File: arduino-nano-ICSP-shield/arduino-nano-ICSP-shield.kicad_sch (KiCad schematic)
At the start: 9 parts, among them J1 Analog, J2 Digital, J3 AVR-ISP-6, J4 Conn_02x04_Counter_Clockwise

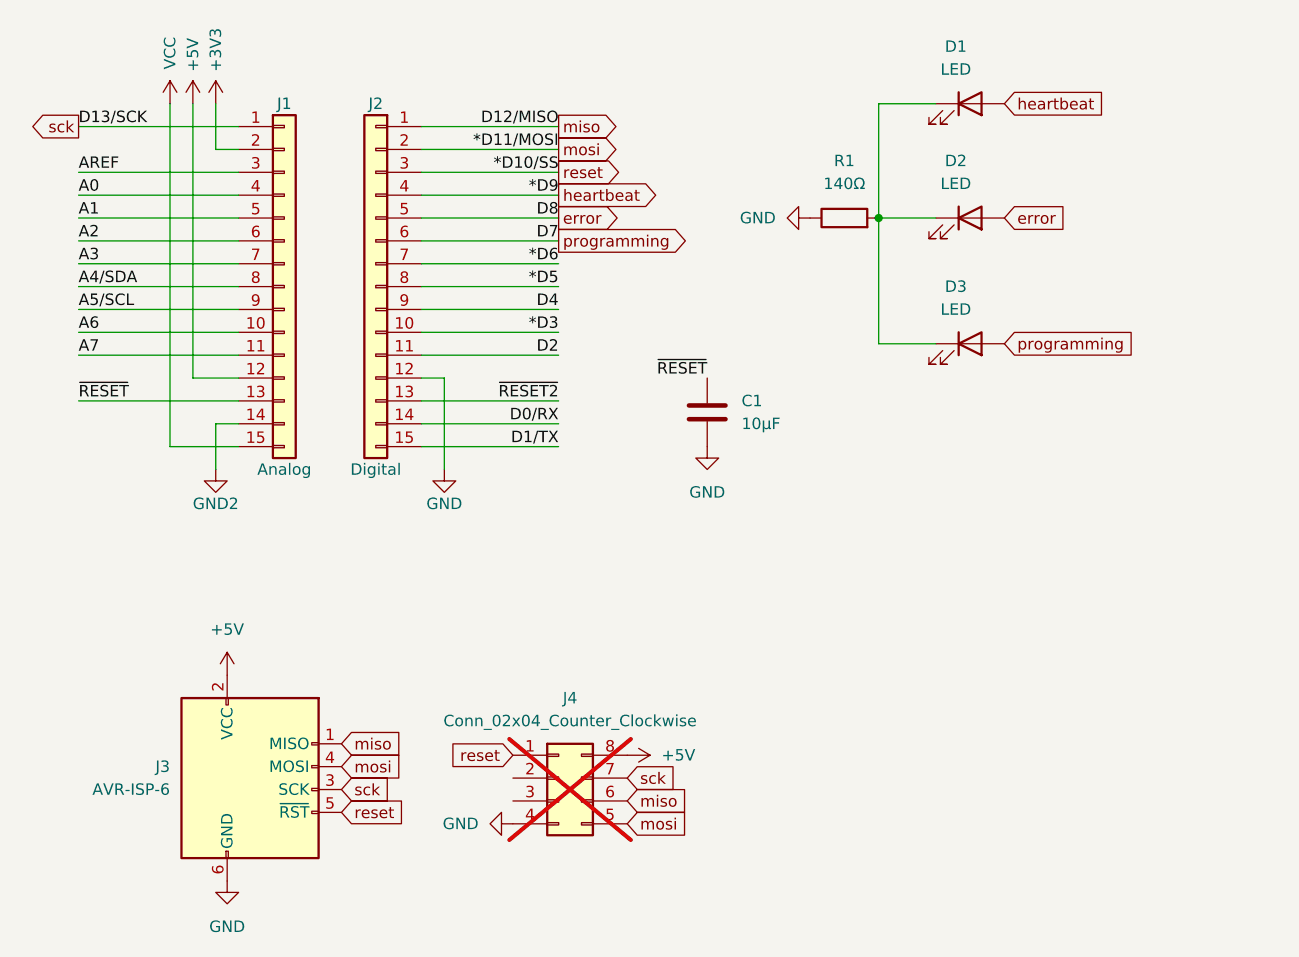
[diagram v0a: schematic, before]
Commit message: add no_connect
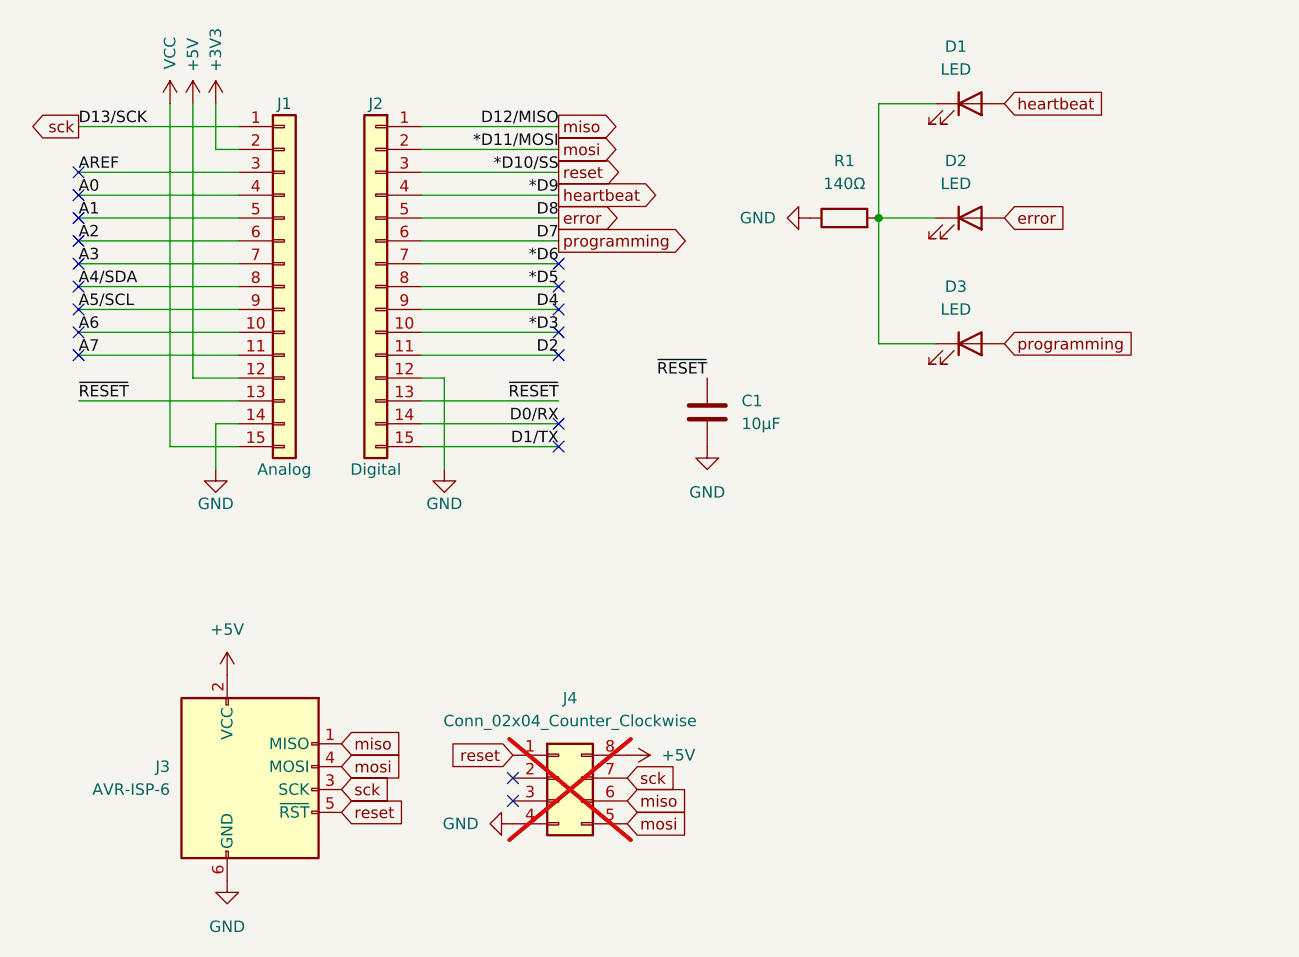
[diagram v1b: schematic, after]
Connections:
- net GND2 is gone; now on net GND: J1.14 (Pin_14)
- net ~{RESET2} is gone; now on net ~{RESET}: J2.13 (Pin_13)
- no-connect marks 0 -> 18
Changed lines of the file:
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@@
 		(color 0 0 0 0)
+	)
+	(no_connect
+		(at 17.78 41.91)
+	)
+	(no_connect
+		(at 71.12 49.53)
+	)
+	(no_connect
+		(at 71.12 41.91)
+	)
+	(no_connect
+		(at 17.78 52.07)
+	)
+	(no_connect
+		(at 71.12 46.99)
+	)
+	(no_connect
+		(at 66.04 99.06)
+	)
+	(no_connect
+		(at 66.04 101.6)
+	)
+	(no_connect
+		(at 71.12 52.07)
+	)
+	(no_connect
+		(at 17.78 49.53)
+	)
+	(no_connect
+		(at 17.78 39.37)
+	)
+	(no_connect
+		(at 17.78 34.29)
+	)
+	(no_connect
+		(at 17.78 46.99)
+	)
+	(no_connect
+		(at 71.12 62.23)
+	)
+	(no_connect
+		(at 71.12 44.45)
+	)
+	(no_connect
+		(at 71.12 59.69)
+	)
+	(no_connect
+		(at 17.78 36.83)
+	)
+	(no_connect
+		(at 17.78 44.45)
+	)
+	(no_connect
+		(at 17.78 31.75)
 	)
 	(wire
@@
 		)
 	)
-	(label "~{RESET2}"
+	(label "~{RESET}"
 		(at 71.12 57.15 180)
 		(effects
@@
 			)
 		)
-		(property "Value" "GND2"
+		(property "Value" "GND"
 			(at 33.02 68.58 0)
 			(effects

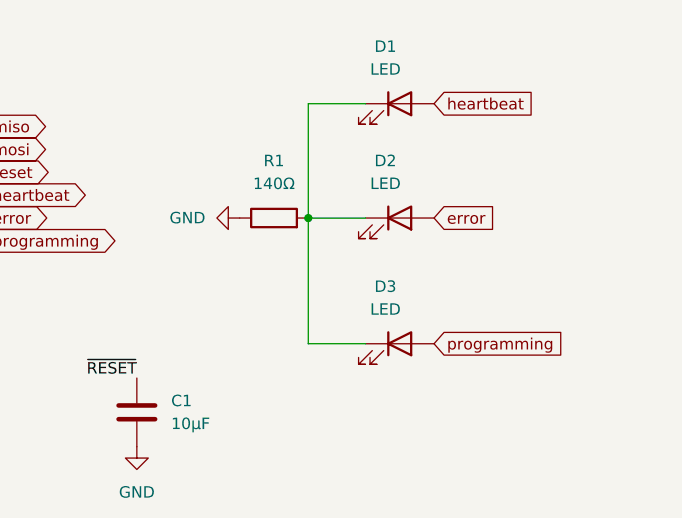
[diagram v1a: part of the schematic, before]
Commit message: 3 different resistors
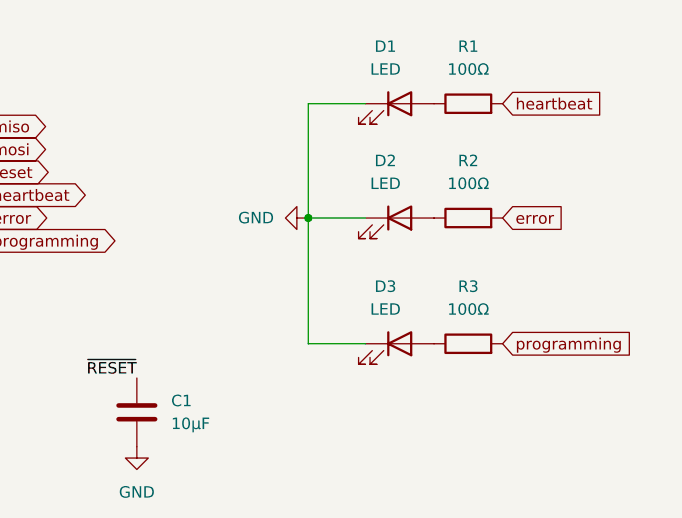
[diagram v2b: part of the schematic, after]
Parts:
- added R2, R3: 100Ω, Resistor_SMD:R_0603_1608Metric, symbol Device:R
- R1: value 140Ω -> 100Ω
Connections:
- net GND: now also D1.1 (K), D2.1 (K), D3.1 (K); no longer R1.1
- net error: now also R2.2; no longer D2.2 (A)
- net heartbeat: now also R1.2; no longer D1.2 (A)
- net programming: now also R3.2; no longer D3.2 (A)
- new net: D3.2 (A), R3.1
- new net: D1.2 (A), R1.1
- new net: D2.2 (A), R2.1
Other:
- moved on the sheet: R1
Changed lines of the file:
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@@
 	(global_label "programming"
 		(shape input)
-		(at 120.65 50.8 0)
+		(at 128.27 50.8 0)
 		(fields_autoplaced yes)
 		(effects
@@
 		)
 		(property "Intersheetrefs" "${INTERSHEET_REFS}"
-			(at 136.1881 50.8 0)
+			(at 143.8081 50.8 0)
 			(effects
 				(font
@@
 	(global_label "heartbeat"
 		(shape input)
-		(at 120.65 24.13 0)
+		(at 128.27 24.13 0)
 		(fields_autoplaced yes)
 		(effects
@@
 		)
 		(property "Intersheetrefs" "${INTERSHEET_REFS}"
-			(at 132.7411 24.13 0)
+			(at 140.3611 24.13 0)
 			(effects
 				(font
@@
 	(global_label "error"
 		(shape input)
-		(at 120.65 36.83 0)
+		(at 128.27 36.83 0)
 		(fields_autoplaced yes)
 		(effects
@@
 		)
 		(property "Intersheetrefs" "${INTERSHEET_REFS}"
-			(at 128.3265 36.83 0)
+			(at 135.9465 36.83 0)
 			(effects
 				(font
@@
 		(on_board yes)
 		(dnp no)
-		(fields_autoplaced yes)
 		(property "Reference" "D1"
 			(at 115.2525 17.78 0)
@@
 	(symbol
 		(lib_id "power:GND")
-		(at 99.06 36.83 270)
+		(at 106.68 36.83 270)
 		(unit 1)
 		(exclude_from_sim no)
@@
 		(fields_autoplaced yes)
 		(property "Reference" "#PWR01"
-			(at 92.71 36.83 0)
+			(at 100.33 36.83 0)
 			(effects
 				(font
@@
 		)
 		(property "Value" "GND"
-			(at 95.25 36.8299 90)
+			(at 102.87 36.8299 90)
 			(effects
 				(font
@@
 		)
 		(property "Footprint" ""
-			(at 99.06 36.83 0)
+			(at 106.68 36.83 0)
 			(effects
 				(font
@@
 		)
 		(property "Datasheet" ""
-			(at 99.06 36.83 0)
+			(at 106.68 36.83 0)
 			(effects
 				(font
@@
 		)
 		(property "Description" "Power symbol creates a global label with name \"GND\" , ground"
-			(at 99.06 36.83 0)
+			(at 106.68 36.83 0)
 			(effects
 				(font
@@
 	(symbol
 		(lib_id "Device:R")
-		(at 102.87 36.83 90)
+		(at 124.46 24.13 90)
 		(unit 1)
 		(exclude_from_sim no)
@@
 		(fields_autoplaced yes)
 		(property "Reference" "R1"
-			(at 102.87 30.48 90)
-			(effects
-				(font
-					(size 1.27 1.27)
-				)
-			)
-		)
-		(property "Value" "140Ω"
-			(at 102.87 33.02 90)
+			(at 124.46 17.78 90)
+			(effects
+				(font
+					(size 1.27 1.27)
+				)
+			)
+		)
+		(property "Value" "100Ω"
+			(at 124.46 20.32 90)
 			(effects
 				(font
@@
 		)
 		(property "Footprint" "Resistor_SMD:R_0603_1608Metric"
-			(at 102.87 38.608 90)
+			(at 124.46 25.908 90)
 			(effects
 				(font
@@
 		)
 		(property "Datasheet" "~"
-			(at 102.87 36.83 0)
+			(at 124.46 24.13 0)
 			(effects
 				(font
@@
 		)
 		(property "Description" "Resistor"
-			(at 102.87 36.83 0)
+			(at 124.46 24.13 0)
 			(effects
 				(font
@@
 					(unit 1)
 				)
+			)
+		)
+	)
+	(symbol
+		(lib_id "Device:R")
+		(at 124.46 36.83 90)
+		(unit 1)
+		(exclude_from_sim no)
+		(in_bom yes)
+		(on_board yes)
+		(dnp no)
+		(fields_autoplaced yes)
+		(property "Reference" "R2"
+			(at 124.46 30.48 90)
+			(effects
+				(font
+					(size 1.27 1.27)
+				)
+			)
+		)
+		(property "Value" "100Ω"
+			(at 124.46 33.02 90)
+			(effects
+				(font
+					(size 1.27 1.27)
+				)
+			)
+		)
+		(property "Footprint" "Resistor_SMD:R_0603_1608Metric"
+			(at 124.46 38.608 90)
+			(effects
+				(font
+					(size 1.27 1.27)
+				)
+				(hide yes)
+			)
+		)
+		(property "Datasheet" "~"
+			(at 124.46 36.83 0)
+			(effects
+				(font
+					(size 1.27 1.27)
+				)
+				(hide yes)
+			)
+		)
+		(property "Description" "Resistor"
+			(at 124.46 36.83 0)
+			(effects
+				(font
+					(size 1.27 1.27)
+				)
+				(hide yes)
+			)
+		)
+		(pin "1"
+		)
+		(pin "2"
+		)
+		(instances
+			(project "arduino-nano-ICSP-shield"
+				(path "/0d35483a-0b12-46cc-b9f2-896fd6831779"
+					(reference "R2")
+					(unit 1)
+				)
+			)
+		)
+	)
+	(symbol
+		(lib_id "Device:R")
+		(at 124.46 50.8 90)
+		(unit 1)
+		(exclude_from_sim no)
+		(in_bom yes)
+		(on_board yes)
+		(dnp no)
+		(fields_autoplaced yes)
+		(property "Reference" "R3"
+			(at 124.46 44.45 90)
+			(effects
+				(font
+					(size 1.27 1.27)
+				)
+			)
+		)
+		(property "Value" "100Ω"
+			(at 124.46 46.99 90)
+			(effects
+				(font
+					(size 1.27 1.27)
+				)
+			)
+		)
+		(property "Footprint" "Resistor_SMD:R_0603_1608Metric"
+			(at 124.46 52.578 90)
+			(effects
+				(font
+					(size 1.27 1.27)
+				)
+				(hide yes)
+			)
+		)
+		(property "Datasheet" "~"
+			(at 124.46 50.8 0)
+			(effects
+				(font
+					(size 1.27 1.27)
+				)
+				(hide yes)
+			)
+		)
+		(property "Description" "Resistor"
+			(at 124.46 50.8 0)
+			(effects
+				(font
+					(size 1.27 1.27)
+				)
+				(hide yes)
+			)
+		)
+		(pin "1"
+		)
+		(pin "2"
+		)
+		(instances
+			(project "arduino-nano-ICSP-shield"
+				(path "/0d35483a-0b12-46cc-b9f2-896fd6831779"
+					(reference "R3")
+					(unit 1)
+				)

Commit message: updated
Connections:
- no-connect marks 18 -> 19
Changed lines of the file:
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@@
+	)
+	(no_connect
+		(at 17.78 57.15)
 	)
 	(no_connect

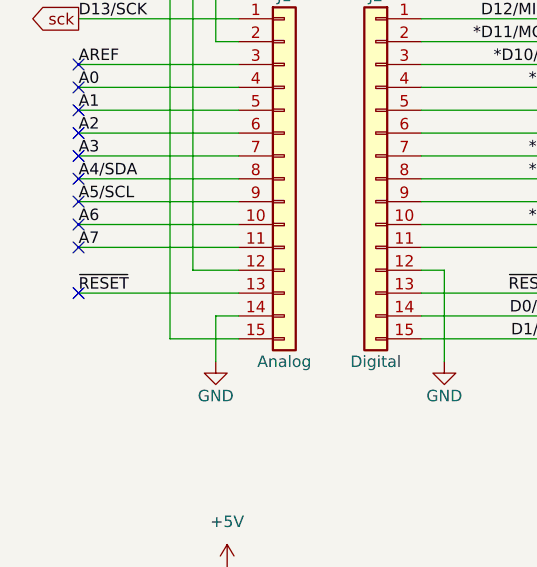
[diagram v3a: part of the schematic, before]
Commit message: split RESET into RESET & RESET2
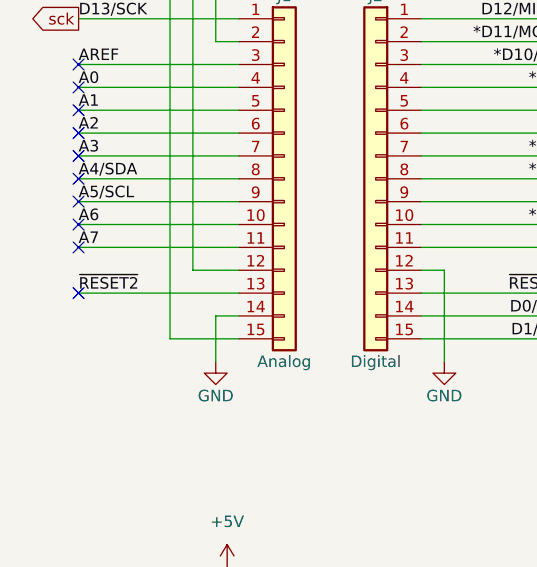
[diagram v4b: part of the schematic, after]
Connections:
- net ~{RESET}: no longer J1.13 (Pin_13)
- new net ~{RESET2}: J1.13 (Pin_13)
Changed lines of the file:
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@@
 		)
 	)
-	(label "~{RESET}"
+	(label "~{RESET2}"
 		(at 17.78 57.15 0)
 		(effects

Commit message: add ttle
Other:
- company: (none) -> MayNiklas
- title: (none) -> Arduino nano ICSP shield
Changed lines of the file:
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@@
 	(paper "A4")
 	(title_block
+		(title "Arduino nano ICSP shield")
 		(date "sam. 04 avril 2015")
+		(rev "1")
+		(company "MayNiklas")
+		(comment 1 "https://github.com/MayNiklas/arduino-nano-ICSP-shield")
 	)
 	(junction

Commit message: add led- to label name
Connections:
- net error renamed led-error
- net heartbeat renamed led-heartbeat
- net programming renamed led-programming
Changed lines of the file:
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@@
 		)
 	)
-	(global_label "error"
+	(global_label "led-error"
 		(shape output)
 		(at 71.12 36.83 0)
@@
 		)
 		(property "Intersheetrefs" "${INTERSHEET_REFS}"
-			(at 78.7965 36.83 0)
+			(at 83.2717 36.83 0)
 			(effects
 				(font
@@
 		)
 	)
-	(global_label "programming"
+	(global_label "led-programming"
 		(shape input)
 		(at 128.27 50.8 0)
@@
 		)
 		(property "Intersheetrefs" "${INTERSHEET_REFS}"
-			(at 143.8081 50.8 0)
-			(effects
-				(font
-					(size 1.27 1.27)
-				)
-				(justify left)
-				(hide yes)
-			)
-		)
-	)
-	(global_label "heartbeat"
+			(at 148.2833 50.8 0)
+			(effects
+				(font
+					(size 1.27 1.27)
+				)
+				(justify left)
+				(hide yes)
+			)
+		)
+	)
+	(global_label "led-heartbeat"
 		(shape output)
 		(at 71.12 34.29 0)
@@
 		)
 		(property "Intersheetrefs" "${INTERSHEET_REFS}"
-			(at 83.2111 34.29 0)
+			(at 87.6863 34.29 0)
 			(effects
 				(font
@@
 		)
 	)
-	(global_label "heartbeat"
+	(global_label "led-heartbeat"
 		(shape input)
 		(at 128.27 24.13 0)
@@
 		)
 		(property "Intersheetrefs" "${INTERSHEET_REFS}"
-			(at 140.3611 24.13 0)
+			(at 144.8363 24.13 0)
 			(effects
 				(font
@@
 		)
 	)
-	(global_label "error"
+	(global_label "led-error"
 		(shape input)
 		(at 128.27 36.83 0)
@@
 		)
 		(property "Intersheetrefs" "${INTERSHEET_REFS}"
-			(at 135.9465 36.83 0)
+			(at 140.4217 36.83 0)
 			(effects
 				(font
@@
 		)
 	)
-	(global_label "programming"
+	(global_label "led-programming"
 		(shape output)
 		(at 71.12 39.37 0)
@@
 		)
 		(property "Intersheetrefs" "${INTERSHEET_REFS}"
-			(at 86.6581 39.37 0)
-			(effects
-				(font
+			(at 91.1333 39.37 0)
+			(effects
+				(font

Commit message: move condensator
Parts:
- R1, R2, R3: value 100Ω -> R
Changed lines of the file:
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@@
 			)
 		)
-		(property "Value" "100Ω"
+		(property "Value" "R"
 			(at 124.46 20.32 90)
 			(effects
@@
 			)
 		)
-		(property "Value" "100Ω"
+		(property "Value" "R"
 			(at 124.46 33.02 90)
 			(effects
@@
 			)
 		)
-		(property "Value" "100Ω"
+		(property "Value" "R"
 			(at 124.46 46.99 90)
 			(effects

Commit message: export project
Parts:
- R1, R2, R3: value R -> 470
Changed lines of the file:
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@@
 			)
 		)
-		(property "Value" "R"
+		(property "Value" "470"
 			(at 124.46 20.32 90)
 			(effects
@@
 			)
 		)
-		(property "Value" "R"
+		(property "Value" "470"
 			(at 124.46 33.02 90)
 			(effects
@@
 			)
 		)
-		(property "Value" "R"
+		(property "Value" "470"
 			(at 124.46 46.99 90)
 			(effects
